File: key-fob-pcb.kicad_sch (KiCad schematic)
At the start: 1 part

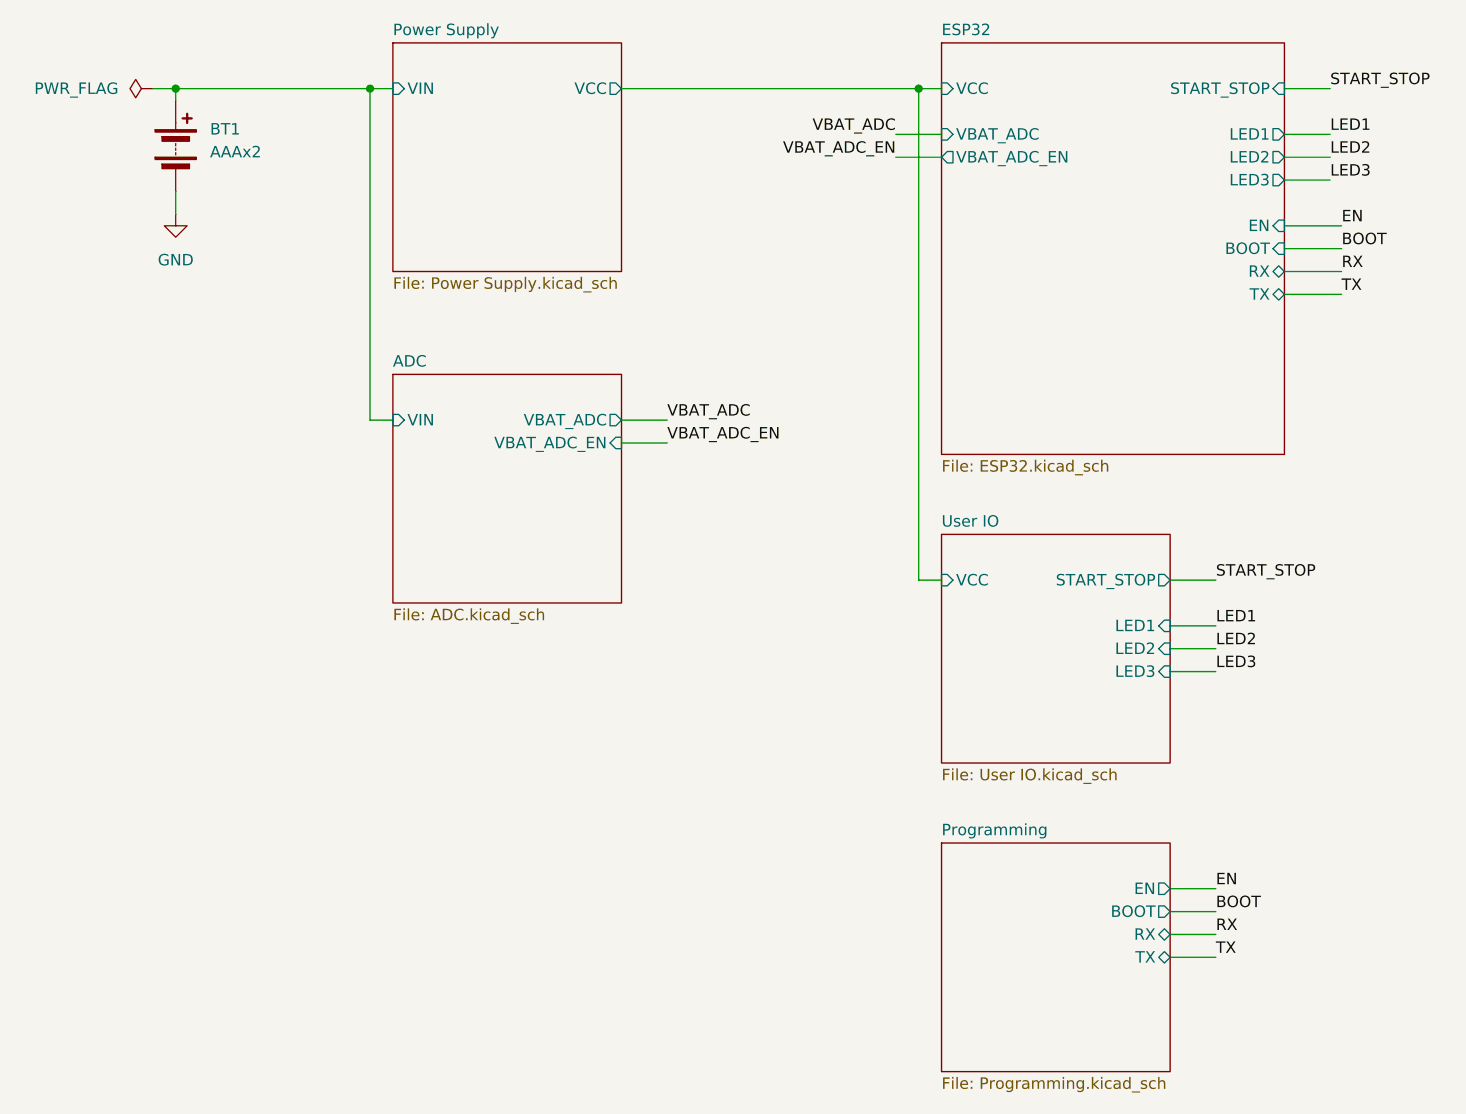
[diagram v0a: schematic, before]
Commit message: switched to full-sized ESP32 S3 WROOM and redid PCB layout
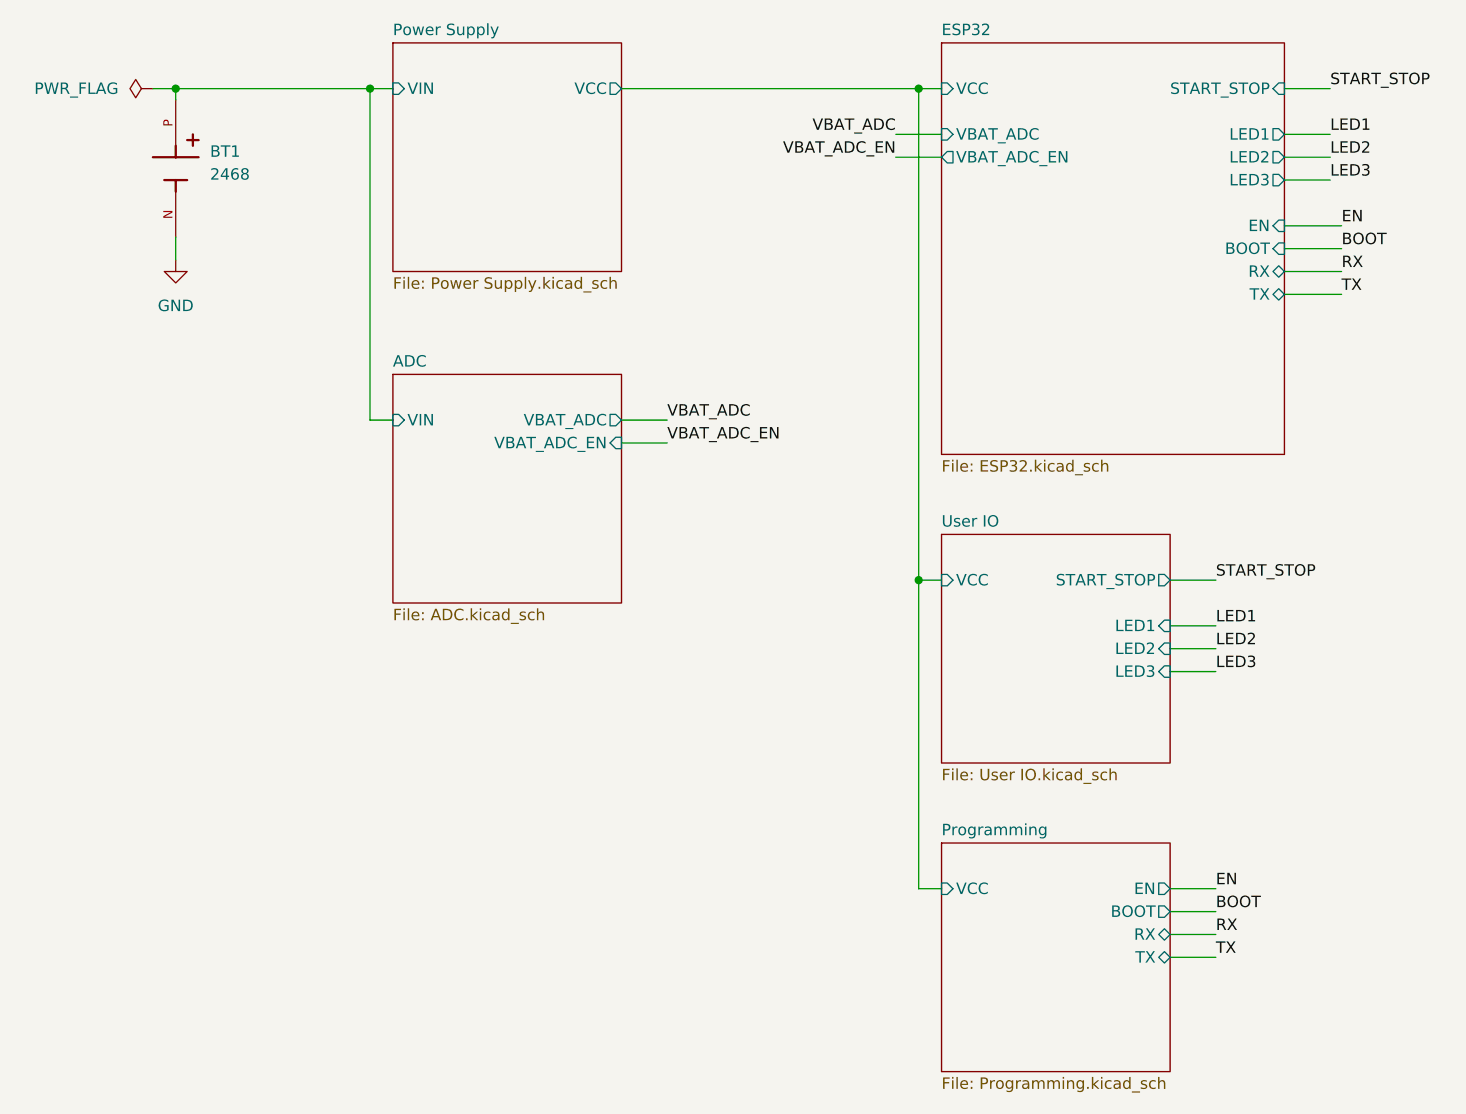
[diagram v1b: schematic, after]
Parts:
- removed BT1: AAAx2, Connector_PinHeader_2.54mm:PinHeader_1x02_P2.54mm_Vertical, symbol Device:Battery
- added BT1: 2468, 2468:BAT_2468, symbol 2468:2468
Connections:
- net ADC/VIN: now also BT1.P
- net GND: now also BT1.N
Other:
- sheet Programming ports: added VCC; removed none
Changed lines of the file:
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@@
     (comment 1 "Author: Ben Martens")
   )
+  (junction (at 144.78 101.6) (diameter 0) (color 0 0 0 0)
+  )
   (junction (at 62.23 46.99) (diameter 0) (color 0 0 0 0)
   )
@@
     (stroke (width 0) (type default))
   )
+  (wire (pts (xy 144.78 135.89) (xy 144.78 101.6))
+    (stroke (width 0) (type default))
+  )
   (wire (pts (xy 111.76 86.36) (xy 116.84 86.36))
     (stroke (width 0) (type default))
@@
     (stroke (width 0) (type default))
   )
+  (wire (pts (xy 147.32 135.89) (xy 144.78 135.89))
+    (stroke (width 0) (type default))
+  )
   (wire (pts (xy 185.42 69.85) (xy 191.77 69.85))
     (stroke (width 0) (type default))
@@
     (stroke (width 0) (type default))
   )
-  (wire (pts (xy 62.23 58.42) (xy 62.23 60.96))
+  (wire (pts (xy 62.23 63.5) (xy 62.23 66.04))
     (stroke (width 0) (type default))
   )
@@
     (effects (font (size 1.27 1.27)) (justify right bottom))
   )
-  (symbol (lib_id "Device:Battery") (at 62.23 53.34 0) (unit 1)
-    (in_bom no) (on_board yes) (dnp no) (fields_autoplaced)
-    (property "Reference" "BT1" (at 66.04 51.4985 0)
-      (effects (font (size 1.27 1.27)) (justify left))
-    )
-    (property "Value" "AAAx2" (at 66.04 54.0385 0)
-      (effects (font (size 1.27 1.27)) (justify left))
-    )
-    (property "Footprint" "Connector_PinHeader_2.54mm:PinHeader_1x02_P2.54mm_Vertical" (at 62.23 51.816 90)
-      (effects (font (size 1.27 1.27)) hide)
-    )
-    (property "Datasheet" "~" (at 62.23 51.816 90)
+  (symbol (lib_id "power:PWR_FLAG") (at 59.69 46.99 90) (unit 1)
+    (in_bom yes) (on_board yes) (dnp no) (fields_autoplaced)
+    (property "Reference" "#FLG01" (at 57.785 46.99 0)
+      (effects (font (size 1.27 1.27)) hide)
+    )
+    (property "Value" "PWR_FLAG" (at 55.88 46.99 90)
+      (effects (font (size 1.27 1.27)) (justify left))
+    )
+    (property "Footprint" "" (at 59.69 46.99 0)
+      (effects (font (size 1.27 1.27)) hide)
+    )
+    (property "Datasheet" "~" (at 59.69 46.99 0)
       (effects (font (size 1.27 1.27)) hide)
     )
     (pin "1")
-    (pin "2")
+    (instances
+      (project "key-fob-pcb"
+        (path "/b002c3bf-fc58-4993-80f7-7914d3aa1ac9"
+          (reference "#FLG01") (unit 1)
+        )
+      )
+    )
+  )
+  (symbol (lib_id "2468:2468") (at 62.23 55.88 270) (unit 1)
+    (in_bom yes) (on_board yes) (dnp no) (fields_autoplaced)
+    (property "Reference" "BT1" (at 66.04 53.975 90)
+      (effects (font (size 1.27 1.27)) (justify left))
+    )
+    (property "Value" "2468" (at 66.04 56.515 90)
+      (effects (font (size 1.27 1.27)) (justify left))
+    )
+    (property "Footprint" "2468:BAT_2468" (at 62.23 55.88 0)
+      (effects (font (size 1.27 1.27)) (justify bottom) hide)
+    )
+    (property "Datasheet" "" (at 62.23 55.88 0)
+      (effects (font (size 1.27 1.27)) hide)
+    )
+    (property "PARTREV" "D" (at 62.23 55.88 0)
+      (effects (font (size 1.27 1.27)) (justify bottom) hide)
+    )
+    (property "STANDARD" "Manufacturer Recommendations" (at 62.23 55.88 0)
+      (effects (font (size 1.27 1.27)) (justify bottom) hide)
+    )
+    (property "SNAPEDA_PN" "2468" (at 62.23 55.88 0)
+      (effects (font (size 1.27 1.27)) (justify bottom) hide)
+    )
+    (property "MAXIMUM_PACKAGE_HEIGHT" "13.25" (at 62.23 55.88 0)
+      (effects (font (size 1.27 1.27)) (justify bottom) hide)
+    )
+    (property "MANUFACTURER" "Keystone" (at 62.23 55.88 0)
+      (effects (font (size 1.27 1.27)) (justify bottom) hide)
+    )
+    (pin "N")
+    (pin "P")
     (instances
       (project "key-fob-pcb"
@@
     )
   )
-  (symbol (lib_id "power:PWR_FLAG") (at 59.69 46.99 90) (unit 1)
+  (symbol (lib_id "power:GND") (at 62.23 66.04 0) (unit 1)
     (in_bom yes) (on_board yes) (dnp no) (fields_autoplaced)
-    (property "Reference" "#FLG01" (at 57.785 46.99 0)
-      (effects (font (size 1.27 1.27)) hide)
-    )
-    (property "Value" "PWR_FLAG" (at 55.88 46.99 90)
-      (effects (font (size 1.27 1.27)) (justify left))
-    )
-    (property "Footprint" "" (at 59.69 46.99 0)
-      (effects (font (size 1.27 1.27)) hide)
-    )
-    (property "Datasheet" "~" (at 59.69 46.99 0)
-      (effects (font (size 1.27 1.27)) hide)
-    )
-    (pin "1")
-    (instances
-      (project "key-fob-pcb"
-        (path "/b002c3bf-fc58-4993-80f7-7914d3aa1ac9"
-          (reference "#FLG01") (unit 1)
-        )
-      )
-    )
-  )
-  (symbol (lib_id "power:GND") (at 62.23 60.96 0) (unit 1)
-    (in_bom yes) (on_board yes) (dnp no) (fields_autoplaced)
-    (property "Reference" "#PWR01" (at 62.23 67.31 0)
-      (effects (font (size 1.27 1.27)) hide)
-    )
-    (property "Value" "GND" (at 62.23 66.04 0)
+    (property "Reference" "#PWR01" (at 62.23 72.39 0)
+      (effects (font (size 1.27 1.27)) hide)
+    )
+    (property "Value" "GND" (at 62.23 71.12 0)
       (effects (font (size 1.27 1.27)))
     )
-    (property "Footprint" "" (at 62.23 60.96 0)
-      (effects (font (size 1.27 1.27)) hide)
-    )
-    (property "Datasheet" "" (at 62.23 60.96 0)
+    (property "Footprint" "" (at 62.23 66.04 0)
+      (effects (font (size 1.27 1.27)) hide)
+    )
+    (property "Datasheet" "" (at 62.23 66.04 0)
       (effects (font (size 1.27 1.27)) hide)
     )
@@
       (effects (font (size 1.27 1.27)) (justify right))
     )
-    (instances
+    (pin "VCC" input (at 147.32 135.89 180)
+      (effects (font (size 1.27 1.27)) (justify left))
+    )
+    (instances
